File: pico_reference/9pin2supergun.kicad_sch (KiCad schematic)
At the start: 11 parts, among them J1 Controller Input, J2 Output, SW1 SW_Wuerth_450301014042, SW2 SW_Push, U1 SN74AVC4T245PW, U2 SN74LVC8T245

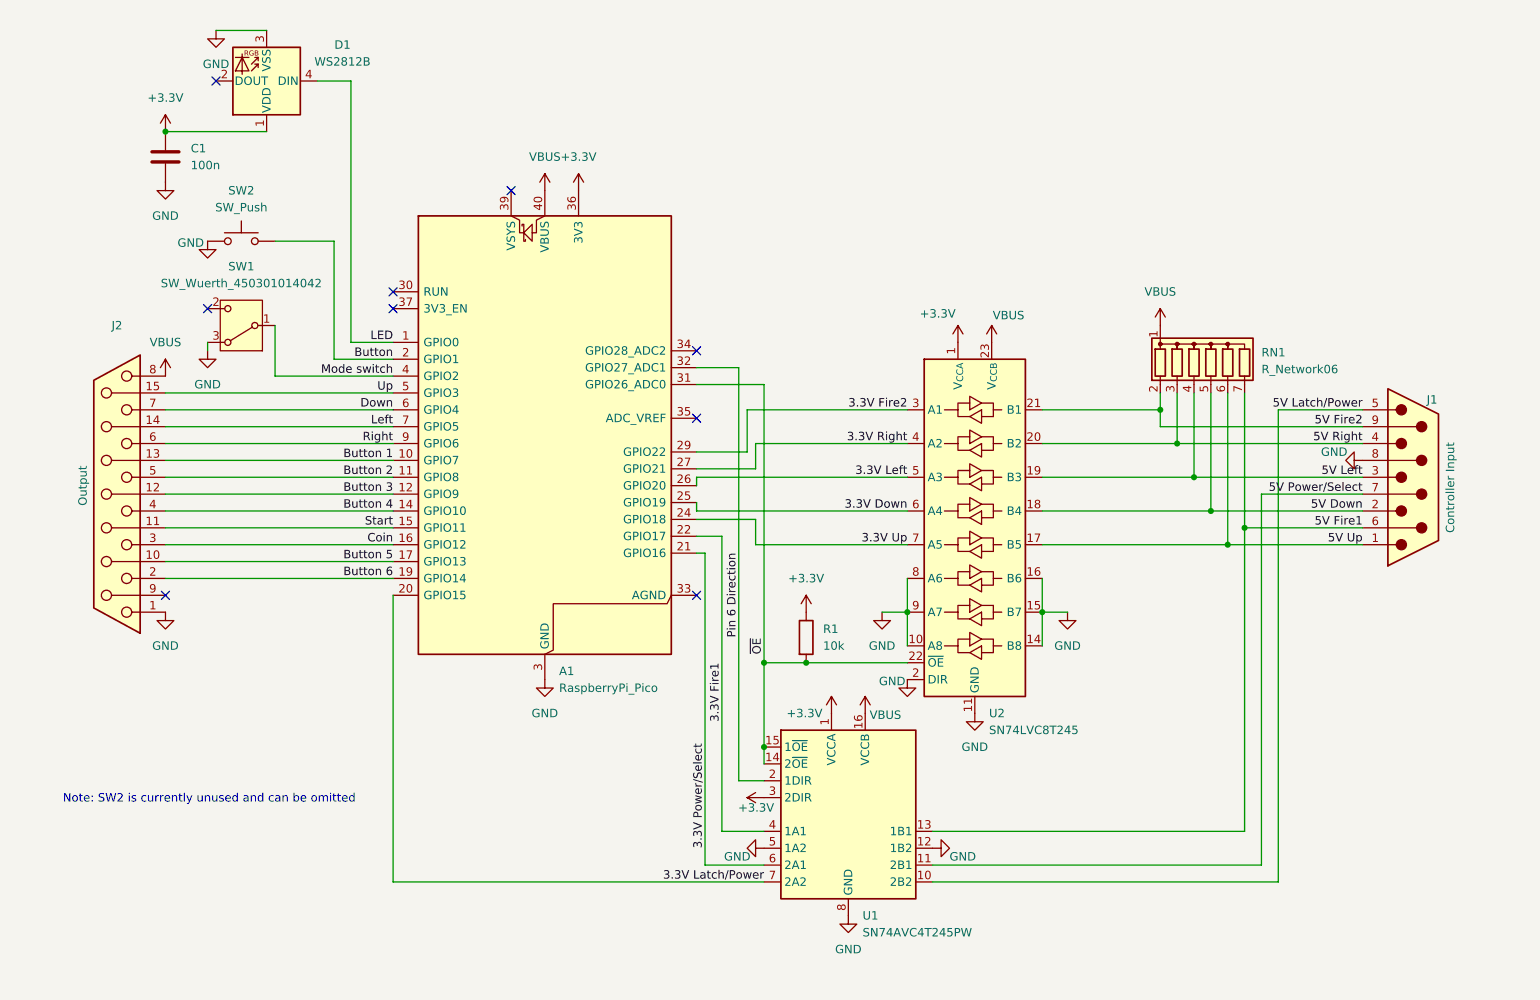
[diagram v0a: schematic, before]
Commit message: Update Pico reference design to use different level shifters
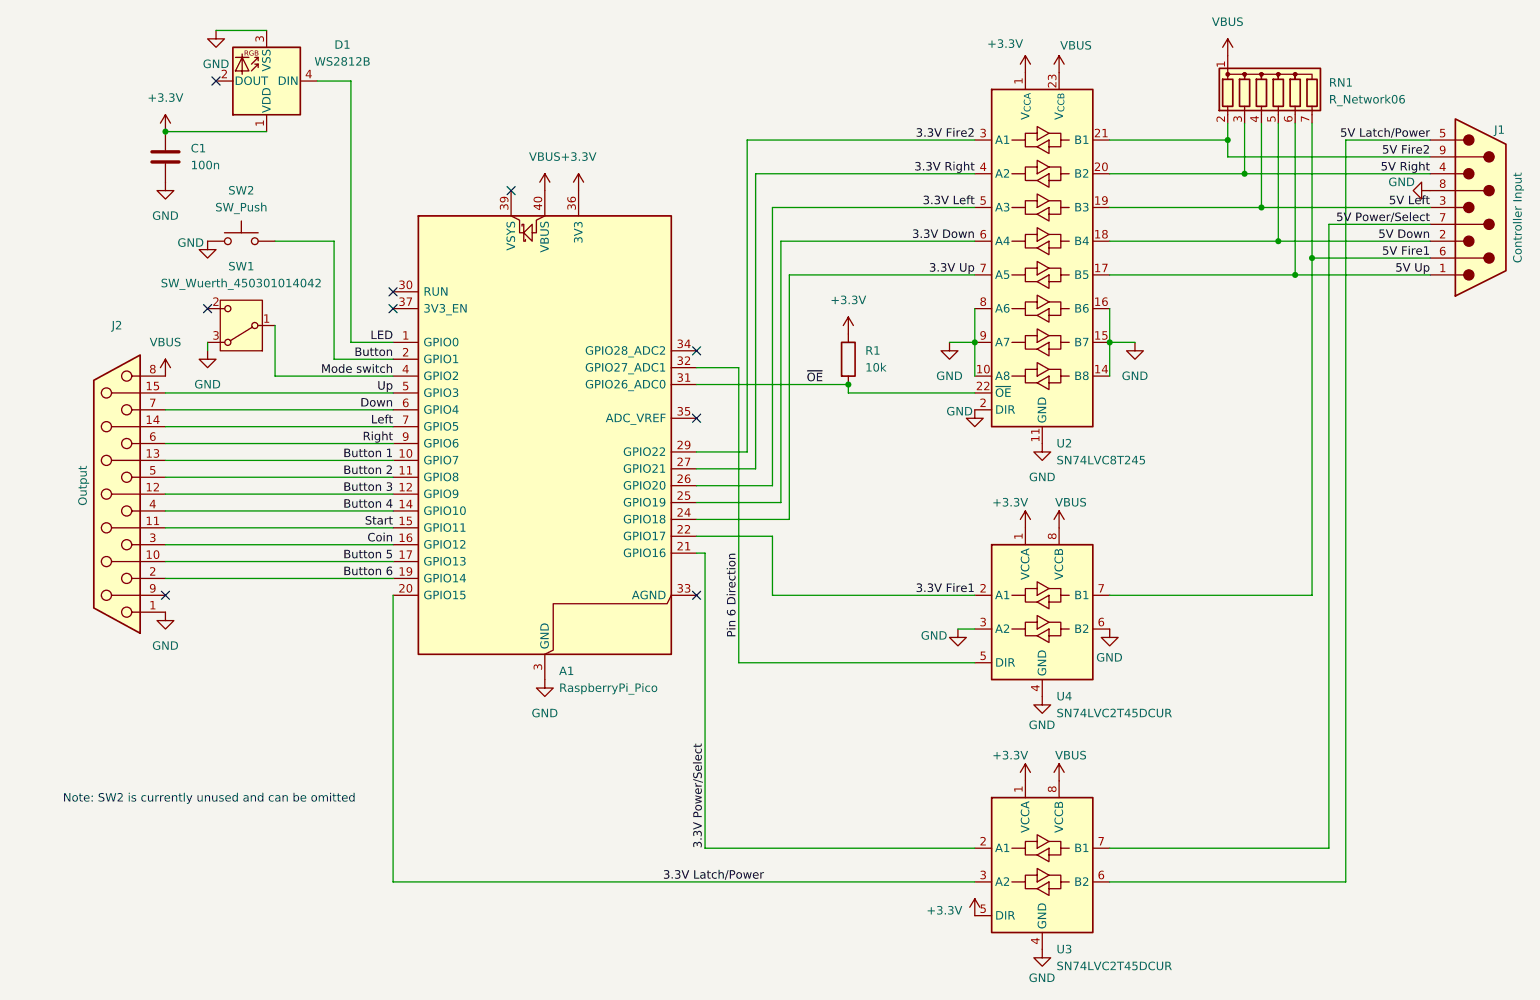
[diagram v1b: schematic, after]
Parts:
- removed U1: SN74AVC4T245PW, Package_SO:TSSOP-16_4.4x5mm_P0.65mm, symbol Logic_LevelTranslator:SN74AVC4T245PW
- added U3, U4: SN74LVC2T45DCUR, Package_SO:VSSOP-8_2.3x2mm_P0.5mm, symbol Logic_LevelTranslator:SN74LVC2T45DCUR
- J2: footprint Connector_Dsub:DSUB-15_Socket_Horizontal_P2.77x2.84mm_EdgePinOffset9.90mm_Housed_MountingHolesOffset11.32mm -> Connector_Dsub:DSUB-15_Socket_Horizontal_P2.77x2.84mm_EdgePinOffset7.70mm_Housed_MountingHolesOffset9.12mm
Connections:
- net +3.3V: now also U3.1 (VCCA), U3.5 (DIR), U4.1 (VCCA)
- net 3.3V Fire1: now also U4.2 (A1)
- net 3.3V Latch/Power: now also U3.3 (A2)
- net 3.3V Power/Select: now also U3.2 (A1)
- net 5V Fire1: now also U4.7 (B1)
- net 5V Latch/Power: now also U3.6 (B2)
- net 5V Power/Select: now also U3.7 (B1)
- net GND: now also U3.4 (GND), U4.3 (A2), U4.4 (GND), U4.6 (B2)
- net Pin 6 Direction: now also U4.5 (DIR)
- net VBUS: now also U3.8 (VCCB), U4.8 (VCCB)
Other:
- moved on the sheet: J1, R1, RN1, U2
